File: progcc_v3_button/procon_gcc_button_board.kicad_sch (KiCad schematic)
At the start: 24 parts, among them J1 Button Board, J2 bumpers, SW1 procon_abxy, SW2 procon_dpad, SW3 TL3315NF100Q, SW4 TL3315NF100Q, SW5 TL3315NF100Q, SW6 TL3315NF100Q

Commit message: Update naming schema
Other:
- company: Luberry's Custom Controllers -> HHL/Esca
- title: Procon GCC Button Board -> ProGCC v3 Button Board
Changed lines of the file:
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@@
   (paper "A")
   (title_block
-    (title "Procon GCC Button Board")
+    (title "ProGCC v3 Button Board")
     (date "2019-12-18")
     (rev "0.2")
-    (company "Luberry's Custom Controllers")
+    (company "HHL/Esca")
   )
   (junction (at 119.38 144.78) (diameter 0) (color 0 0 0 0)

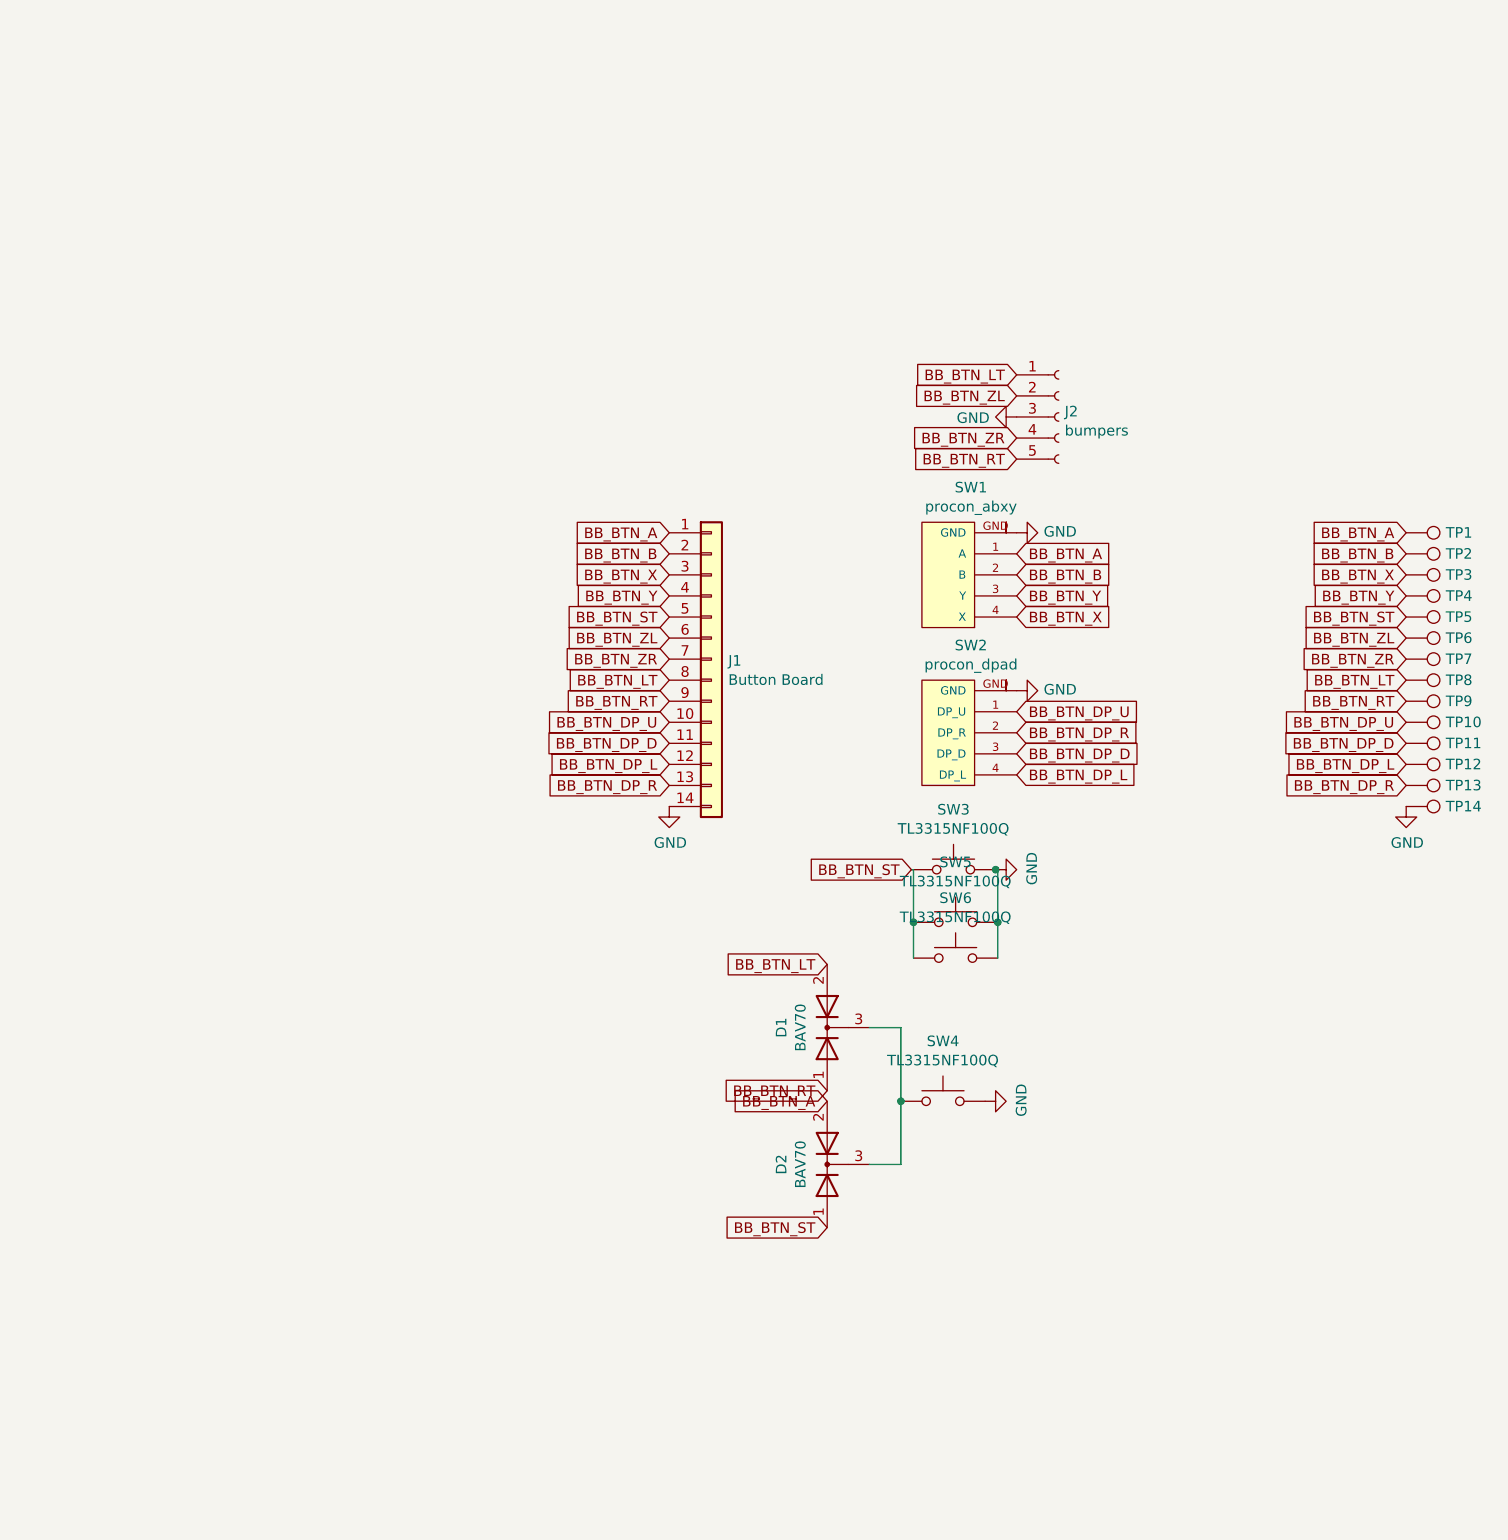
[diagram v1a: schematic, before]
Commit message: Update button board
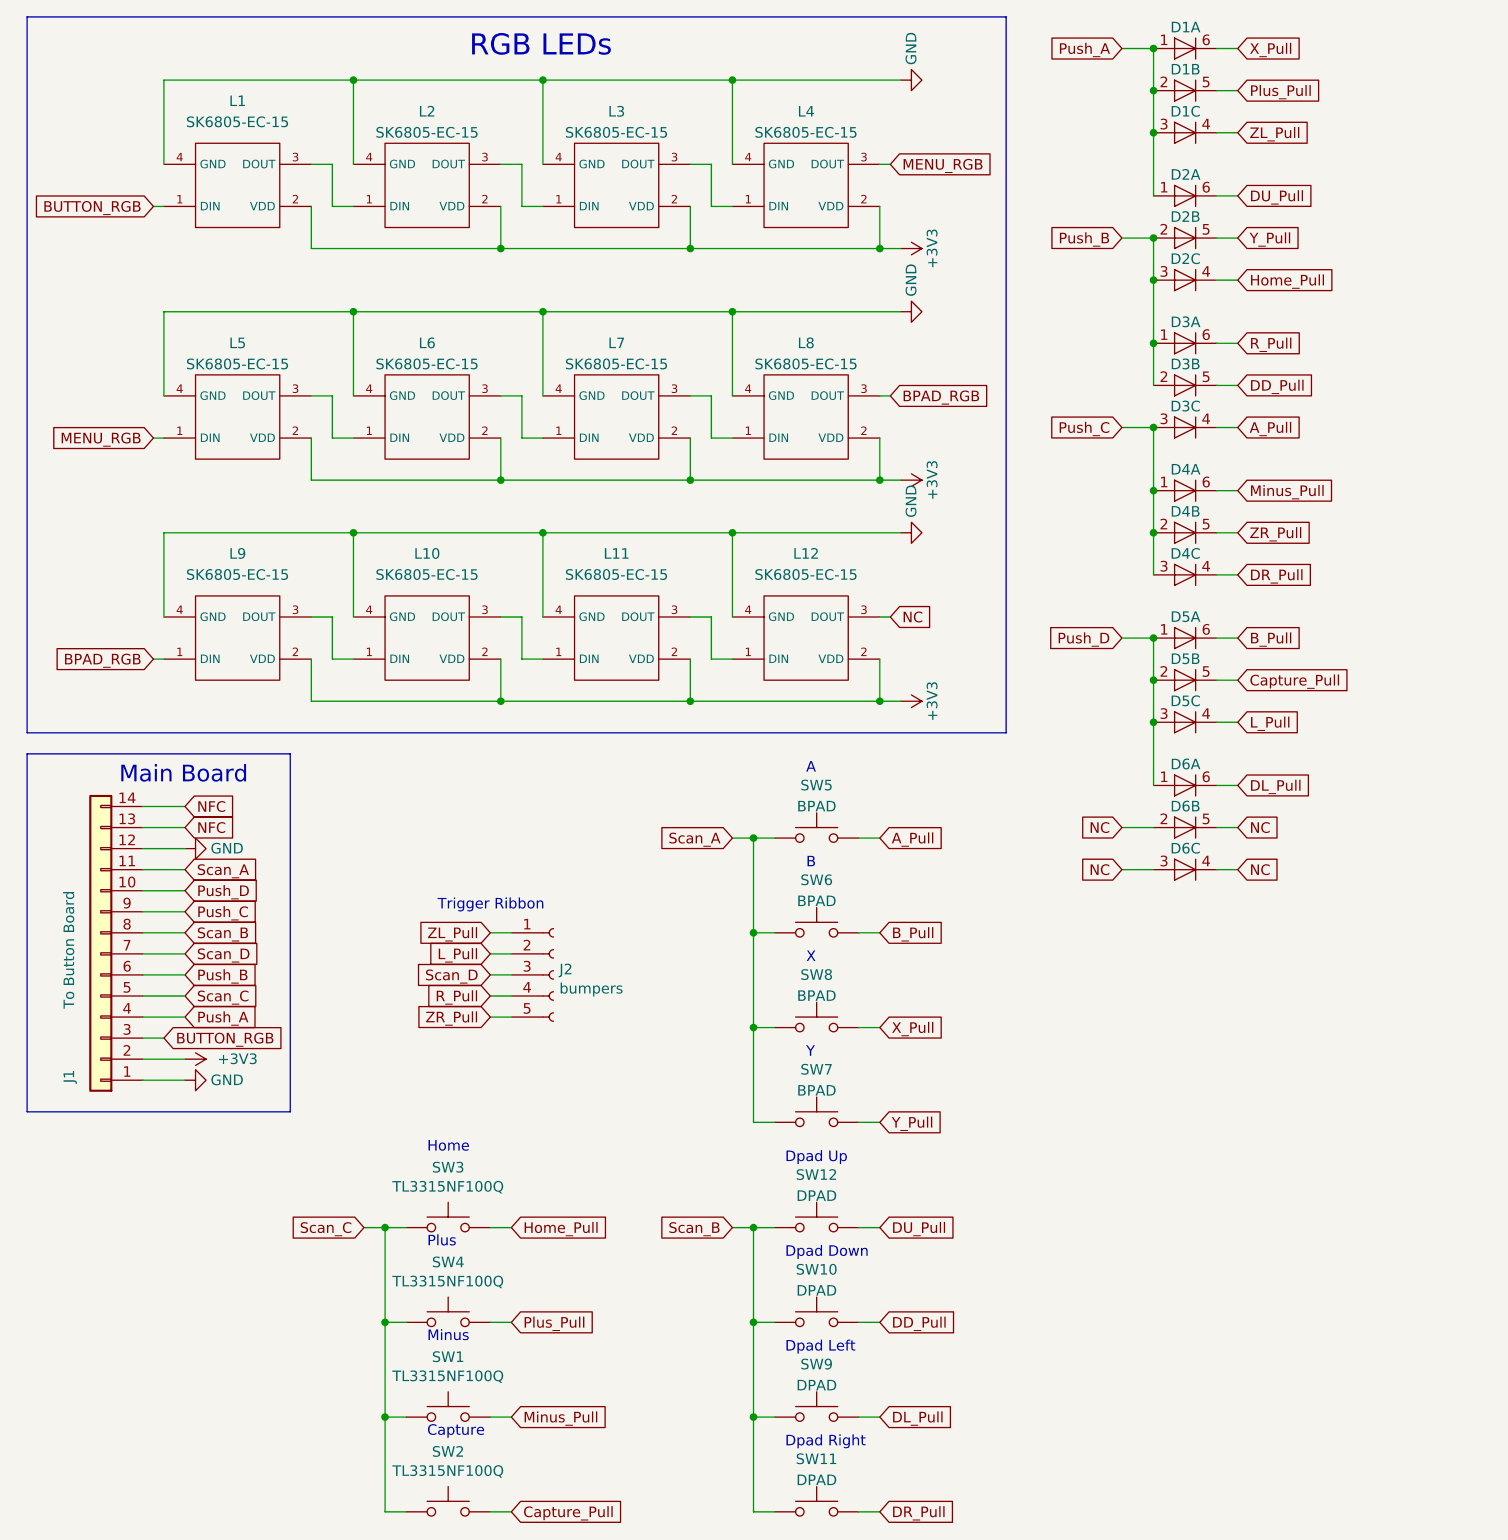
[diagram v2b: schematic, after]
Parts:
- removed D1, D2: BAV70, Package_TO_SOT_SMD:SOT-23, symbol Diode:BAV70
- removed SW1: procon_abxy, procon_gcc:procon_abxy, symbol gcc:procon_abxy
- removed SW2: procon_dpad, procon_gcc:procon_dpad, symbol gcc:procon_dpad
- removed TP1, TP10, TP11, TP12, TP13, TP14, TP2, TP3, TP4, TP5, TP6, TP7, TP8, TP9: TestPoint, TestPoint:TestPoint_Pad_D1.5mm, symbol Connector:TestPoint
- added D1, D2, D3, D4, D5, D6: BAS16VY,115, Package_TO_SOT_SMD:SOT-363_SC-70-6, symbol progcc_v3:BAS16VY,115
- added L1, L10, L11, L12, L2, L3, L4, L5, L6, L7, L8, L9: SK6805-EC-15, progcc_v3:SK6805-EC-15, symbol progcc_v3:SK6805-EC-15
- added SW10, SW11, SW12, SW9: DPAD, progcc_v3:progcc_dpad, symbol Switch:SW_Push
- added SW5, SW6, SW7, SW8: BPAD, progcc_v3:progcc_bpad, symbol Switch:SW_Push
- J1: value Button Board -> To Button Board; footprint procon_gcc:molex_5051101492_14P -> progcc_v3:molex_5051101492_14P
- J2: footprint procon_gcc:molex_5051100592_5P -> progcc_v3:molex_5051100592_5P
- SW1: renamed from SW5; footprint procon_gcc:TL3315NFxxxQ -> progcc_v3:TL3315NFxxxQ; symbol Switch:SW_Push -> progcc_v3:SW_Quad
- SW2: renamed from SW4; footprint procon_gcc:TL3315NFxxxQ -> progcc_v3:TL3315NFxxxQ; symbol Switch:SW_Push -> progcc_v3:SW_Quad
- SW3: renamed from SW6; footprint procon_gcc:TL3315NFxxxQ -> progcc_v3:TL3315NFxxxQ; symbol Switch:SW_Push -> progcc_v3:SW_Quad
- SW4: renamed from SW3; footprint procon_gcc:TL3315NFxxxQ -> progcc_v3:TL3315NFxxxQ; symbol Switch:SW_Push -> progcc_v3:SW_Quad
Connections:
- net BB_BTN_A is gone; now on net GND: J1.1 (Pin_1)
- net BB_BTN_DP_L is gone; now on net GND: J1.12 (Pin_12)
- net BB_BTN_ST is gone; now on net Scan_C: J1.5 (Pin_5), SW1.1, SW3.1, SW4.1
- net GND: now also L1.4 (GND), L10.4 (GND), L11.4 (GND), L12.4 (GND), L2.4 (GND), L3.4 (GND), L4.4 (GND), L5.4 (GND), L6.4 (GND), L7.4 (GND), L8.4 (GND), L9.4 (GND); no longer J1.14 (Pin_14), J2.3 (Pin_3), SW1.2, SW2.2, SW3.2, SW4.2
- net Scan_C: now reaches SW2.1
- net Scan_C: now also SW1.2, SW2.2, SW3.2, SW4.2
- net BB_BTN_B renamed +3V3
- net +3V3: now also L1.2 (VDD), L10.2 (VDD), L11.2 (VDD), L12.2 (VDD), L2.2 (VDD), L3.2 (VDD), L4.2 (VDD), L5.2 (VDD), L6.2 (VDD), L7.2 (VDD), L8.2 (VDD), L9.2 (VDD)
- net BB_BTN_DP_D renamed Scan_A
- net Scan_A: now also SW5.1, SW6.1, SW7.1, SW8.1
- net BB_BTN_DP_R renamed NFC
- net NFC: now also J1.14 (Pin_14)
- net BB_BTN_DP_U renamed Push_D
- net Push_D: now also D5.1 (A), D5.2 (A), D5.3 (A), D6.1 (A)
- net BB_BTN_LT renamed Scan_B
- net Scan_B: now also SW10.1, SW11.1, SW12.1, SW9.1; no longer J2.1 (Pin_1)
- net BB_BTN_RT renamed Push_C
- net Push_C: now also D3.3 (A), D4.1 (A), D4.2 (A), D4.3 (A); no longer J2.5 (Pin_5)
- net BB_BTN_X renamed BUTTON_RGB
- net BUTTON_RGB: now also L1.1 (DIN)
- net BB_BTN_Y renamed Push_A
- net Push_A: now also D1.1 (A), D1.2 (A), D1.3 (A), D2.1 (A)
- net BB_BTN_ZL renamed L_Pull
- net L_Pull: now also D5.4 (K); no longer J1.6 (Pin_6)
- net BB_BTN_ZR renamed R_Pull
- net R_Pull: now also D3.6 (K); no longer J1.7 (Pin_7)
- new net: L10.1 (DIN), L9.3 (DOUT)
- new net: L10.3 (DOUT), L11.1 (DIN)
- new net: L1.3 (DOUT), L2.1 (DIN)
- new net: L2.3 (DOUT), L3.1 (DIN)
- new net: L11.3 (DOUT), L12.1 (DIN)
- new net: L6.3 (DOUT), L7.1 (DIN)
- new net: L7.3 (DOUT), L8.1 (DIN)
- new net: L5.3 (DOUT), L6.1 (DIN)
- new net: L3.3 (DOUT), L4.1 (DIN)
- new net A_Pull: D3.4 (K), SW5.2
- new net BPAD_RGB: L8.3 (DOUT), L9.1 (DIN)
- new net B_Pull: D5.6 (K), SW6.2
- new net Capture_Pull: D5.5 (K), SW2.3, SW2.4
- new net DD_Pull: D3.5 (K), SW10.2
- new net DL_Pull: D6.6 (K), SW9.2
- new net DR_Pull: D4.4 (K), SW11.2
- new net DU_Pull: D2.6 (K), SW12.2
- new net Home_Pull: D2.4 (K), SW3.3, SW3.4
- new net MENU_RGB: L4.3 (DOUT), L5.1 (DIN)
- new net Minus_Pull: D4.6 (K), SW1.3, SW1.4
- new net NC: D6.2 (A), D6.3 (A), D6.4 (K), D6.5 (K), L12.3 (DOUT)
- new net Plus_Pull: D1.5 (K), SW4.3, SW4.4
- new net Push_B: D2.2 (A), D2.3 (A), D3.1 (A), D3.2 (A), J1.6 (Pin_6)
- new net Scan_D: J1.7 (Pin_7), J2.3 (Pin_3)
- new net X_Pull: D1.6 (K), SW8.2
- new net Y_Pull: D2.5 (K), SW7.2
- new net ZL_Pull: D1.4 (K), J2.1 (Pin_1)
- new net ZR_Pull: D4.5 (K), J2.5 (Pin_5)
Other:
- note added: "A"
- note added: "B"
- note added: "Capture"
- note added: "Dpad Down"
- note added: "Dpad Left"
- note added: "Dpad Right"
- note added: "Dpad Up"
- note added: "Home"
- note added: "Main Board"
- note added: "Minus"
- note added: "Plus"
- note added: "RGB LEDs"
- note added: "Trigger Ribbon"
- note added: "X"
- note added: "Y"
- moved on the sheet: SW1, SW2, SW3, SW4

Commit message: Update proto
- Update stick position
- Adjust some screw position slightly
- Fix schematic for Crystal and Rumble
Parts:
- J2: footprint progcc_v3:molex_5051100592_5P -> progcc_v3:molex_5034800540
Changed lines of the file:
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@@
       (effects (font (size 1.27 1.27)) (justify left))
     )
-    (property "Footprint" "progcc_v3:molex_5051100592_5P" (at 77.47 129.54 0)
+    (property "Footprint" "progcc_v3:molex_5034800540" (at 77.47 129.54 0)
       (effects (font (size 1.27 1.27)) hide)
     )

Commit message: Major updates
-Revised button board outline
-Added IMU for motion
-Cleaned up traces on main board
-Add test pads to button board
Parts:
- D1, D2, D3, D4, D5, D6: footprint Package_TO_SOT_SMD:SOT-363_SC-70-6 -> progcc_v3:SOT-363_SC-70-6
- J2: MPN (none) -> molex_5034800540
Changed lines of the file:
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@@
+      (effects (font (size 1.27 1.27)) hide)
+    )
+    (property "MPN" "molex_5034800540" (at 77.47 129.54 0)
       (effects (font (size 1.27 1.27)) hide)
     )
@@
       (effects (font (size 1.27 1.27)) hide)
     )
-    (property "Footprint" "Package_TO_SOT_SMD:SOT-363_SC-70-6" (at 153.67 118.11 0)
+    (property "Footprint" "progcc_v3:SOT-363_SC-70-6" (at 153.67 118.11 0)
       (effects (font (size 1.27 1.27)) hide)
     )
@@
       (effects (font (size 1.27 1.27)) hide)
     )
-    (property "Footprint" "Package_TO_SOT_SMD:SOT-363_SC-70-6" (at 153.67 113.03 0)
+    (property "Footprint" "progcc_v3:SOT-363_SC-70-6" (at 153.67 113.03 0)
       (effects (font (size 1.27 1.27)) hide)
     )
@@
       (effects (font (size 1.27 1.27)) hide)
     )
-    (property "Footprint" "Package_TO_SOT_SMD:SOT-363_SC-70-6" (at 153.67 34.29 0)
+    (property "Footprint" "progcc_v3:SOT-363_SC-70-6" (at 153.67 34.29 0)
       (effects (font (size 1.27 1.27)) hide)
     )
@@
       (effects (font (size 1.27 1.27)) hide)
     )
-    (property "Footprint" "Package_TO_SOT_SMD:SOT-363_SC-70-6" (at 153.67 64.77 0)
+    (property "Footprint" "progcc_v3:SOT-363_SC-70-6" (at 153.67 64.77 0)
       (effects (font (size 1.27 1.27)) hide)
     )
@@
       (effects (font (size 1.27 1.27)) hide)
     )
-    (property "Footprint" "Package_TO_SOT_SMD:SOT-363_SC-70-6" (at 153.67 41.91 0)
+    (property "Footprint" "progcc_v3:SOT-363_SC-70-6" (at 153.67 41.91 0)
       (effects (font (size 1.27 1.27)) hide)
     )
@@
       (effects (font (size 1.27 1.27)) hide)
     )
-    (property "Footprint" "Package_TO_SOT_SMD:SOT-363_SC-70-6" (at 153.67 69.85 0)
+    (property "Footprint" "progcc_v3:SOT-363_SC-70-6" (at 153.67 69.85 0)
       (effects (font (size 1.27 1.27)) hide)
     )
@@
       (effects (font (size 1.27 1.27)) hide)
     )
-    (property "Footprint" "Package_TO_SOT_SMD:SOT-363_SC-70-6" (at 153.67 77.47 0)
+    (property "Footprint" "progcc_v3:SOT-363_SC-70-6" (at 153.67 77.47 0)
       (effects (font (size 1.27 1.27)) hide)
     )
@@
       (effects (font (size 1.27 1.27)) hide)
     )
-    (property "Footprint" "Package_TO_SOT_SMD:SOT-363_SC-70-6" (at 153.67 87.63 0)
+    (property "Footprint" "progcc_v3:SOT-363_SC-70-6" (at 153.67 87.63 0)
       (effects (font (size 1.27 1.27)) hide)
     )
@@
       (effects (font (size 1.27 1.27)) hide)
     )
-    (property "Footprint" "Package_TO_SOT_SMD:SOT-363_SC-70-6" (at 153.67 46.99 0)
+    (property "Footprint" "progcc_v3:SOT-363_SC-70-6" (at 153.67 46.99 0)
       (effects (font (size 1.27 1.27)) hide)
     )
@@
       (effects (font (size 1.27 1.27)) hide)
     )
-    (property "Footprint" "Package_TO_SOT_SMD:SOT-363_SC-70-6" (at 153.67 29.21 0)
+    (property "Footprint" "progcc_v3:SOT-363_SC-70-6" (at 153.67 29.21 0)
       (effects (font (size 1.27 1.27)) hide)
     )
@@
       (effects (font (size 1.27 1.27)) hide)
     )
-    (property "Footprint" "Package_TO_SOT_SMD:SOT-363_SC-70-6" (at 153.67 52.07 0)
+    (property "Footprint" "progcc_v3:SOT-363_SC-70-6" (at 153.67 52.07 0)
       (effects (font (size 1.27 1.27)) hide)
     )
@@
       (effects (font (size 1.27 1.27)) hide)
     )
-    (property "Footprint" "Package_TO_SOT_SMD:SOT-363_SC-70-6" (at 153.67 100.33 0)
+    (property "Footprint" "progcc_v3:SOT-363_SC-70-6" (at 153.67 100.33 0)
       (effects (font (size 1.27 1.27)) hide)
     )
@@
       (effects (font (size 1.27 1.27)) hide)
     )
-    (property "Footprint" "Package_TO_SOT_SMD:SOT-363_SC-70-6" (at 153.67 123.19 0)
+    (property "Footprint" "progcc_v3:SOT-363_SC-70-6" (at 153.67 123.19 0)
       (effects (font (size 1.27 1.27)) hide)
     )
@@
       (effects (font (size 1.27 1.27)) hide)
     )
-    (property "Footprint" "Package_TO_SOT_SMD:SOT-363_SC-70-6" (at 153.67 95.25 0)
+    (property "Footprint" "progcc_v3:SOT-363_SC-70-6" (at 153.67 95.25 0)
       (effects (font (size 1.27 1.27)) hide)
     )
@@
       (effects (font (size 1.27 1.27)) hide)
     )
-    (property "Footprint" "Package_TO_SOT_SMD:SOT-363_SC-70-6" (at 153.67 59.69 0)
+    (property "Footprint" "progcc_v3:SOT-363_SC-70-6" (at 153.67 59.69 0)
       (effects (font (size 1.27 1.27)) hide)
     )
@@
       (effects (font (size 1.27 1.27)) hide)
     )
-    (property "Footprint" "Package_TO_SOT_SMD:SOT-363_SC-70-6" (at 153.67 82.55 0)
+    (property "Footprint" "progcc_v3:SOT-363_SC-70-6" (at 153.67 82.55 0)
       (effects (font (size 1.27 1.27)) hide)
     )
@@
       (effects (font (size 1.27 1.27)) hide)
     )
-    (property "Footprint" "Package_TO_SOT_SMD:SOT-363_SC-70-6" (at 153.67 24.13 0)
+    (property "Footprint" "progcc_v3:SOT-363_SC-70-6" (at 153.67 24.13 0)
       (effects (font (size 1.27 1.27)) hide)
     )
@@
       (effects (font (size 1.27 1.27)) hide)
     )
-    (property "Footprint" "Package_TO_SOT_SMD:SOT-363_SC-70-6" (at 153.67 105.41 0)
-      (effects (font (size 1.27 1.27)) hide)
-    )
+    (property "Footprint" "progcc_v3:SOT-363_SC-70-6" (at 153.67 105.41 0)
+      (effects (font (size 1.27 1.27)) hide)
+    )
